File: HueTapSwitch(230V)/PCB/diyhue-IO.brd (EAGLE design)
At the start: 45.5 x 45.5 mm, 43 parts, among them IC1 MCP1825T-3302E/DC, X1 DG129-5.0, X2 DG129-5.0, X3 DG129-5.0

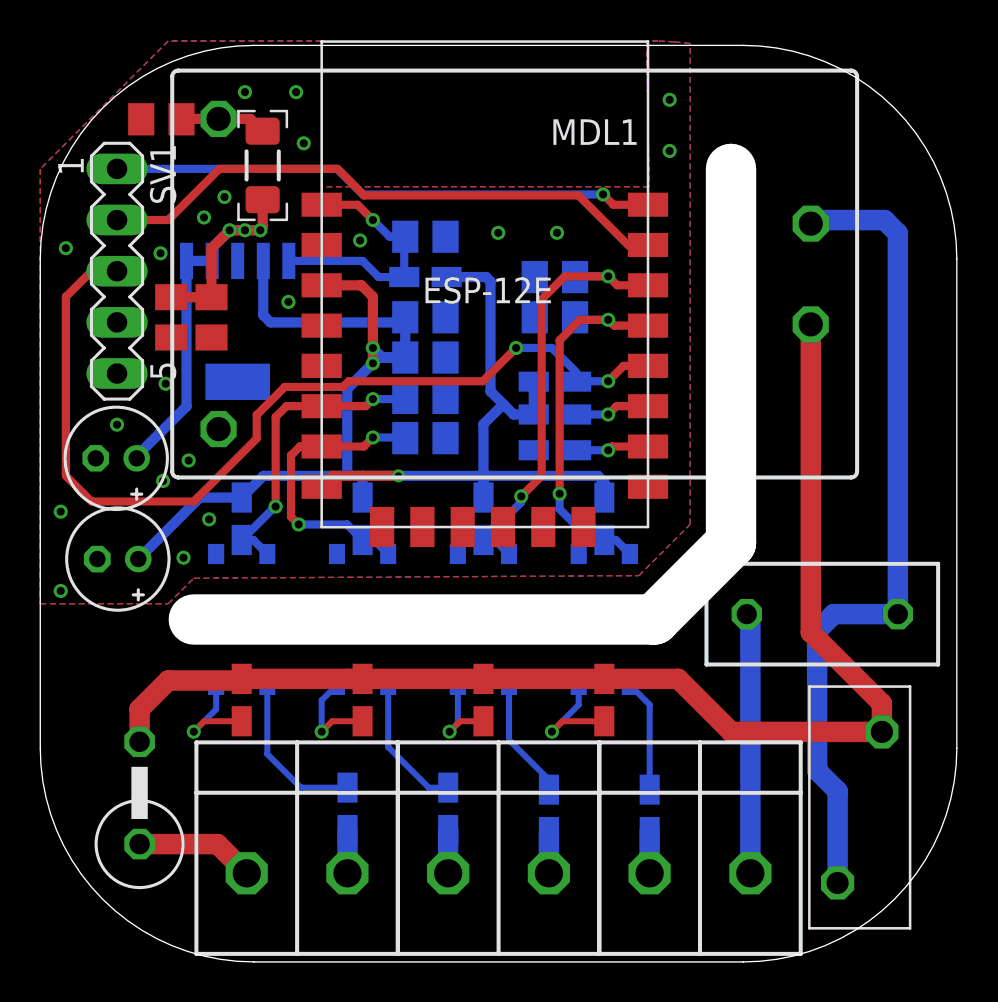
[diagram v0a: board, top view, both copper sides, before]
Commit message: changed Resistors on the inputs from 0805 to 1210
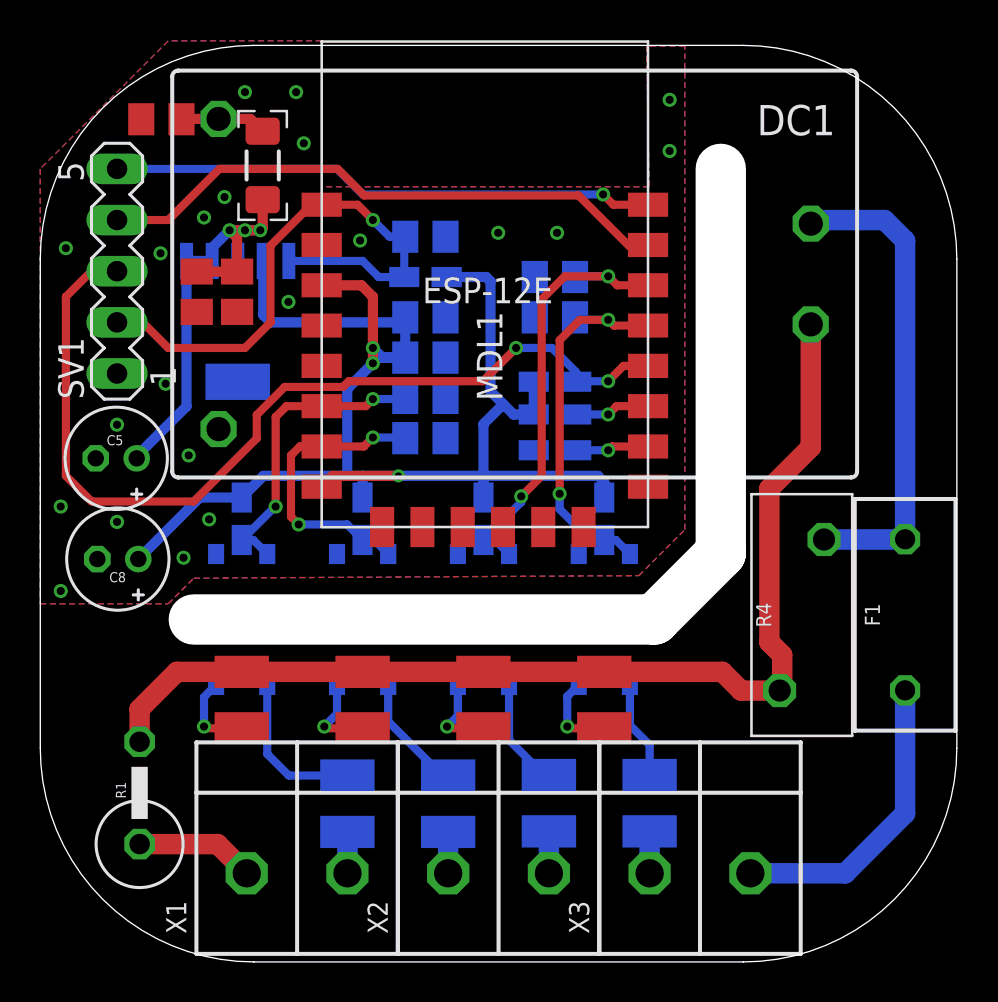
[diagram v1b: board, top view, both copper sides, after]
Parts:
- R10, R13, R14, R5, R6, R7, R8, R9: device rcl:R0805W -> rcl:R1210
- moved R4 9.97 mm to (37.8, 17.2), turned to 90 degrees
- moved F1 4.11 mm to (42.9, 17.2), turned to 90 degrees
- moved C11 1.80 mm to (9.77, 33.3)
- moved C7 1.80 mm to (7.77, 33.3)
- moved R14 0.38 mm to (30.2, 7.88)
- moved R5 0.38 mm to (25.2, 7.88)
- moved R7 0.25 mm to (15.2, 7.85)
- moved R8 0.25 mm to (20.2, 7.85)
- turned SV1 to 90 degrees
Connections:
- net !RST: now also SV1.2
- net GND: now also SV1.1; no longer SV1.4, SV1.5
- net RX: now also SV1.4; no longer SV1.2
- net TX: now also SV1.5; no longer SV1.1
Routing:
- net N$2: track 40.9 -> 24.0 mm
- net !RST: track 12.9 -> 28.8 mm
- net HV.COM: track 61.9 -> 53.9 mm
- net HV.L: track 12.9 -> 15.0 mm
- net N$13: track 5.69 -> 4.17 mm
- net +5V: track 24.3 -> 22.8 mm
- net N$16: track 5.37 -> 4.22 mm
- net N$19: track 6.90 -> 5.90 mm
- net N$14: track 5.60 -> 4.87 mm
- net N$17: track 4.88 -> 4.27 mm
- net N$20: track 6.02 -> 5.43 mm
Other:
- outline, holes or cut-outs redrawn
- board text added: "4x Input 2019 Philipp Hunger"
- board text removed: "4x Input (C) 2019 Philipp Hunger"
